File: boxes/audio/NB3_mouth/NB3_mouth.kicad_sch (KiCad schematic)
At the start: 3 parts, among them IC1 MAX98357AETE+T, J1 Conn_02x03_Odd_Even, J2 Conn_02x03_Odd_Even

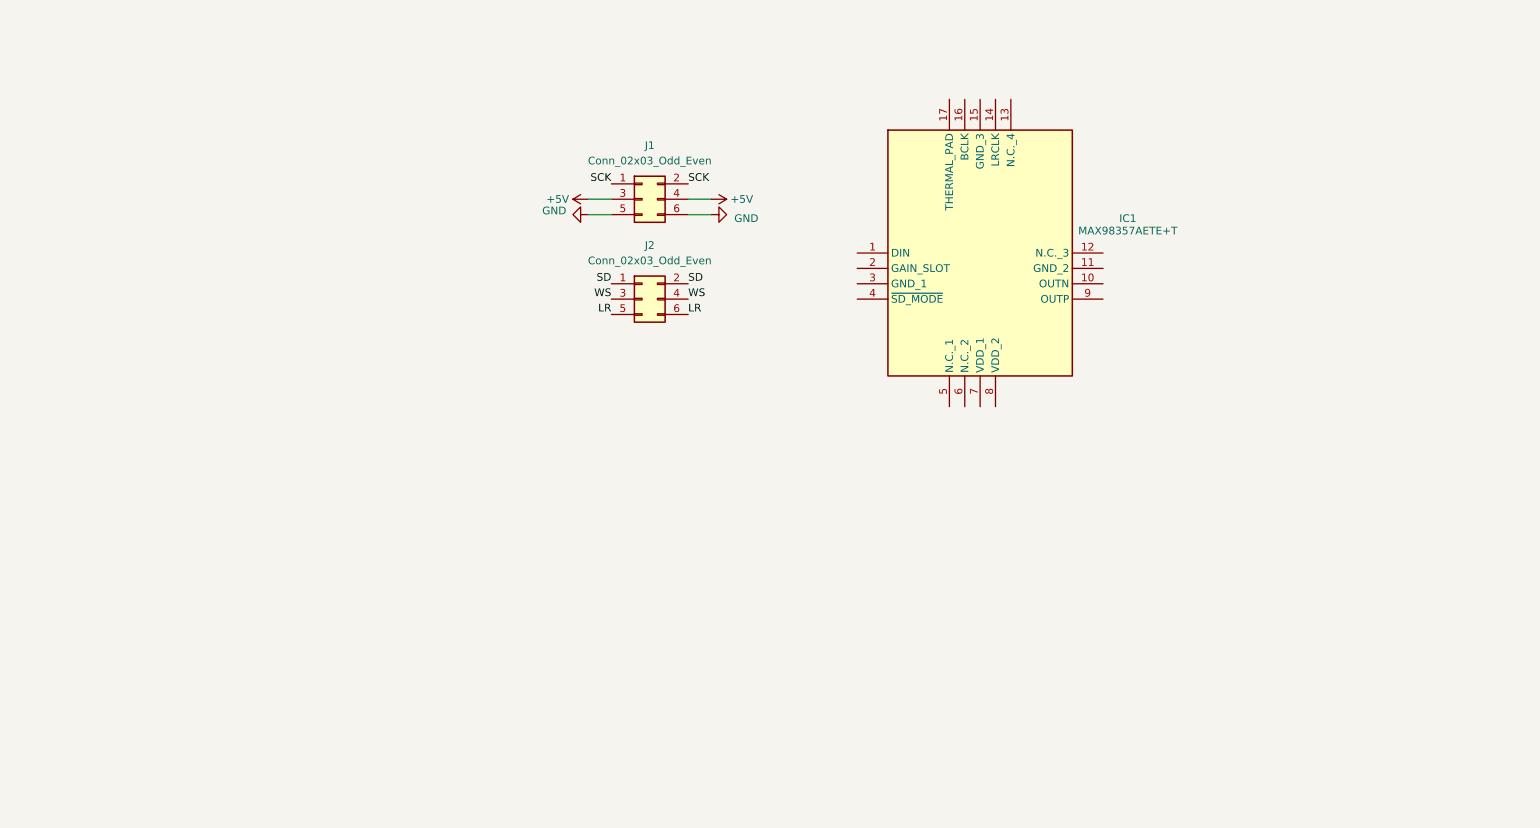
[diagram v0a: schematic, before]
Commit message: Tweak NB3_mouth
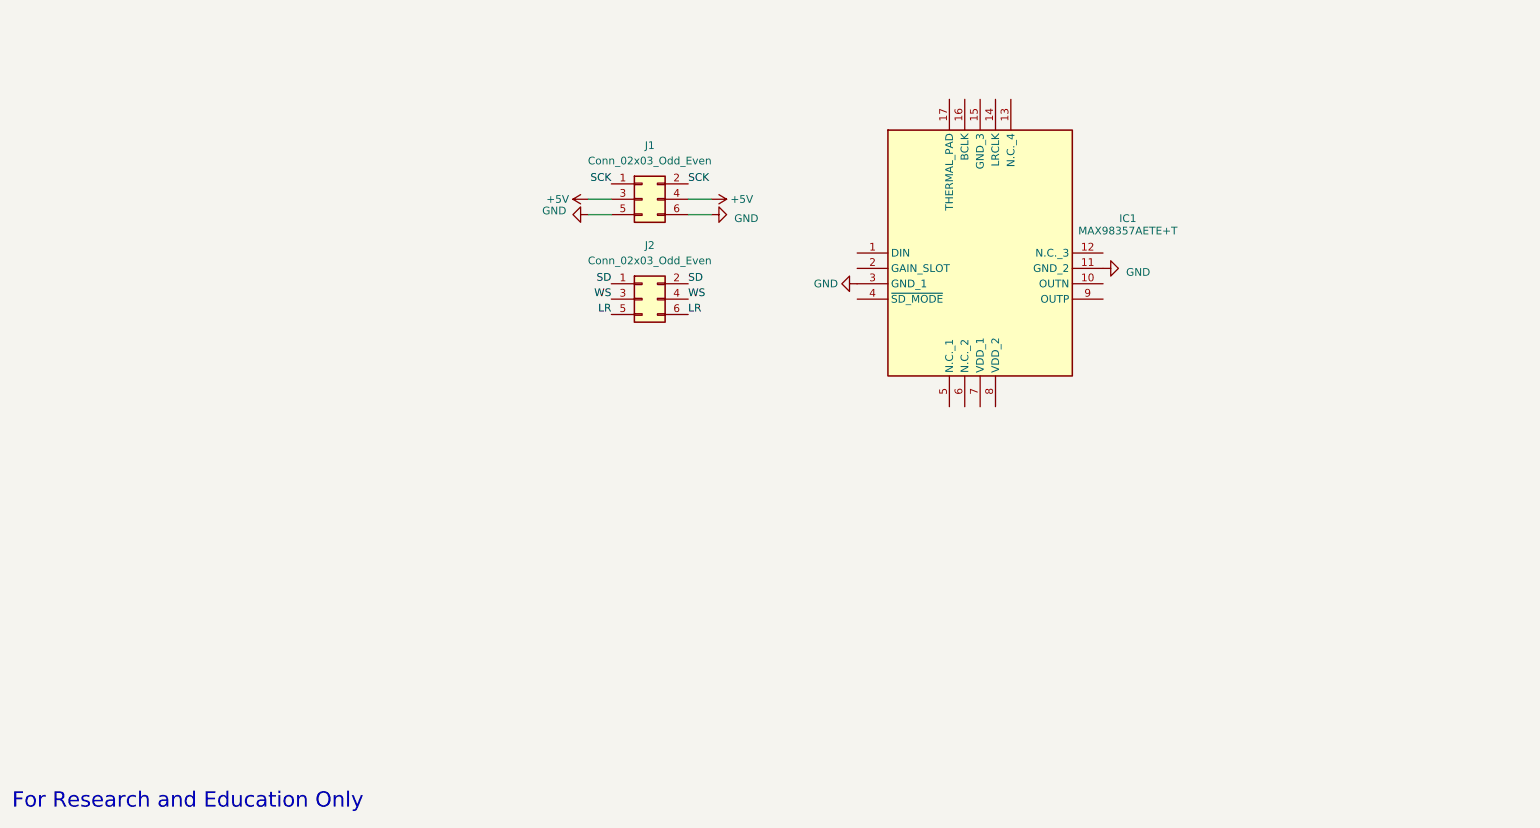
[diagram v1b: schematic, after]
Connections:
- net GND: now also IC1.11 (GND_2), IC1.3 (GND_1)
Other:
- note added: "For Research and Education Only"
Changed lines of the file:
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@@
     (stroke (width 0) (type solid))
   )
+  (text "For Research and Education Only" (at 15.24 194.945 0)
+    (effects (font (size 2.54 2.54) (color 0 0 0 1)) (justify left bottom))
+  )
   (label "LR" (at 114.3 113.03 180) (fields_autoplaced)
     (effects (font (size 1.27 1.27)) (justify right bottom))
@@
   (label "WS" (at 127 110.49 0) (fields_autoplaced)
     (effects (font (size 1.27 1.27)) (justify left bottom))
+  )
+  (symbol (lib_id "power:GND") (at 154.94 107.95 270) (unit 1)
+    (in_bom yes) (on_board yes) (dnp no) (fields_autoplaced)
+    (property "Reference" "#PWR06" (at 148.59 107.95 0)
+      (effects (font (size 1.27 1.27)) hide)
+    )
+    (property "Value" "GND" (at 151.7651 107.95 90)
+      (effects (font (size 1.27 1.27)) (justify right))
+    )
+    (property "Footprint" "" (at 154.94 107.95 0)
+      (effects (font (size 1.27 1.27)) hide)
+    )
+    (property "Datasheet" "" (at 154.94 107.95 0)
+      (effects (font (size 1.27 1.27)) hide)
+    )
+    (pin "1")
+    (instances
+      (project "NB3_mouth"
+        (path "/df27637c-d6c9-48ad-83e5-144198b72706"
+          (reference "#PWR06") (unit 1)
+        )
+      )
+    )
   )
   (symbol (lib_id "NB3_mouth:I2S_DAC-AMP_MAX98357A") (at 154.94 102.87 0) (unit 1)
@@
         )
       )
+    )
+  )
+  (symbol (lib_id "power:GND") (at 195.58 105.41 90) (unit 1)
+    (in_bom yes) (on_board yes) (dnp no) (fields_autoplaced)
+    (property "Reference" "#PWR05" (at 201.93 105.41 0)
+      (effects (font (size 1.27 1.27)) hide)
+    )
+    (property "Value" "GND" (at 199.39 106.0449 90)
+      (effects (font (size 1.27 1.27)) (justify right))
+    )
+    (property "Footprint" "" (at 195.58 105.41 0)
+      (effects (font (size 1.27 1.27)) hide)
+    )
+    (property "Datasheet" "" (at 195.58 105.41 0)
+      (effects (font (size 1.27 1.27)) hide)
+    )
+    (pin "1")
+    (instances
+      (project "NB3_mouth"
+        (path "/df27637c-d6c9-48ad-83e5-144198b72706"
+          (reference "#PWR05") (unit 1)
+        )
+      )

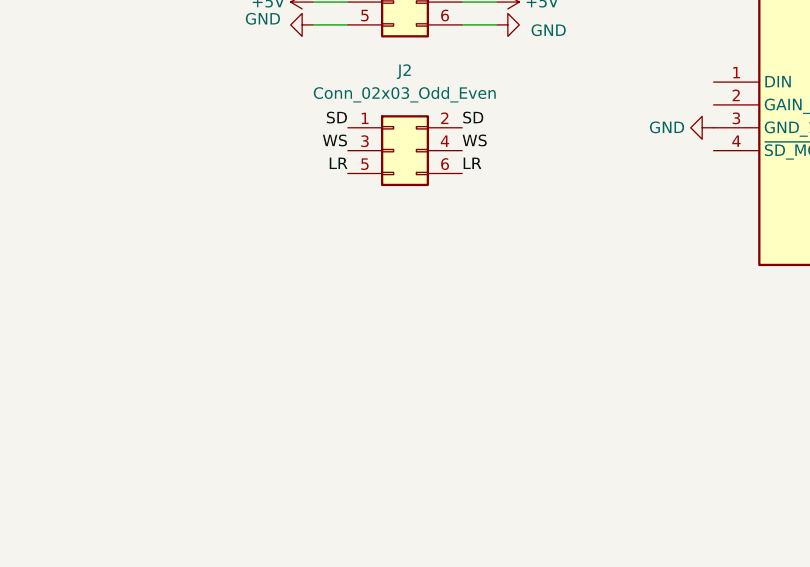
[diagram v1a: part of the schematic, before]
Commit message: Add JST connector to NB3_mouth
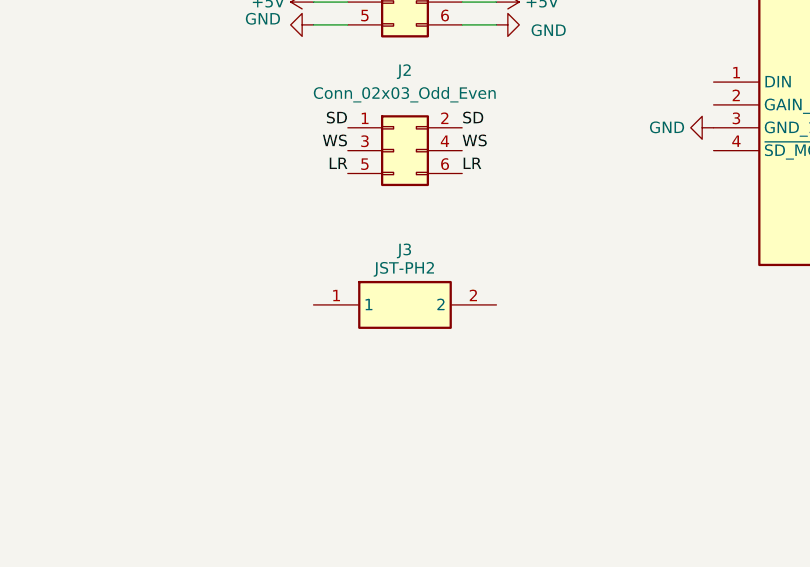
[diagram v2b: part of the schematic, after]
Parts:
- added J3: JST-PH2, NB3_mouth:Connector_Female_JST-PH2, symbol NB3_mouth:Connector_Female_JST-PH2
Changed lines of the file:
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@@
+    )
+  )
+  (symbol (lib_id "NB3_mouth:Connector_Female_JST-PH2") (at 110.49 127.635 0) (unit 1)
+    (in_bom yes) (on_board yes) (dnp no) (fields_autoplaced)
+    (property "Reference" "J3" (at 120.65 121.515 0)
+      (effects (font (size 1.27 1.27)))
+    )
+    (property "Value" " JST-PH2" (at 120.65 123.563 0)
+      (effects (font (size 1.27 1.27)))
+    )
+    (property "Footprint" "NB3_mouth:Connector_Female_JST-PH2" (at 127 222.555 0)
+      (effects (font (size 1.27 1.27)) (justify left top) hide)
+    )
+    (property "Datasheet" "https://cdn-shop.adafruit.com/datasheets/17311.pdf" (at 127 322.555 0)
+      (effects (font (size 1.27 1.27)) (justify left top) hide)
+    )
+    (property "Height" "" (at 127 522.555 0)
+      (effects (font (size 1.27 1.27)) (justify left top) hide)
+    )
+    (property "Mouser Part Number" "485-1769" (at 127 622.555 0)
+      (effects (font (size 1.27 1.27)) (justify left top) hide)
+    )
+    (property "Mouser Price/Stock" "https://www.mouser.co.uk/ProductDetail/Adafruit/1769?qs=GURawfaeGuBbgoGtf2XstA%3D%3D" (at 127 722.555 0)
+      (effects (font (size 1.27 1.27)) (justify left top) hide)
+    )
+    (property "Manufacturer_Name" "Adafruit" (at 127 822.555 0)
+      (effects (font (size 1.27 1.27)) (justify left top) hide)
+    )
+    (property "Manufacturer_Part_Number" "1769" (at 127 922.555 0)
+      (effects (font (size 1.27 1.27)) (justify left top) hide)
+    )
+    (pin "1")
+    (pin "2")
+    (instances
+      (project "NB3_mouth"
+        (path "/df27637c-d6c9-48ad-83e5-144198b72706"
+          (reference "J3") (unit 1)
+        )
+      )
     )
   )

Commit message: Upload NB3_ear "fab" v2
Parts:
- added R1, R2: R, Resistor_SMD:R_0402_1005Metric, symbol Device:R
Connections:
- net LR is gone; now on net Gain: J2.5 (Pin_5), J2.6 (Pin_6)
- net +5V: now also IC1.7 (VDD_1), IC1.8 (VDD_2), R1.1
- net GND: now also IC1.15 (GND_3), IC1.17 (THERMAL_PAD), R2.1
- net SCK: now also IC1.16 (BCLK)
- net SD: now also IC1.1 (DIN)
- net WS: now also IC1.14 (LRCLK)
- net Speaker-: now reaches IC1.10 (OUTN)
- net Speaker-: now also J3.2
- net Gain: now reaches IC1.2 (GAIN_SLOT)
- net at IC1.4 (~{SD_MODE}): now also R1.2, R2.2
- net Speaker+: now reaches IC1.9 (OUTP)
- net Speaker+: now also J3.1
- no-connect marks 0 -> 4
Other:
- moved on the sheet: IC1, J1, J2, J3

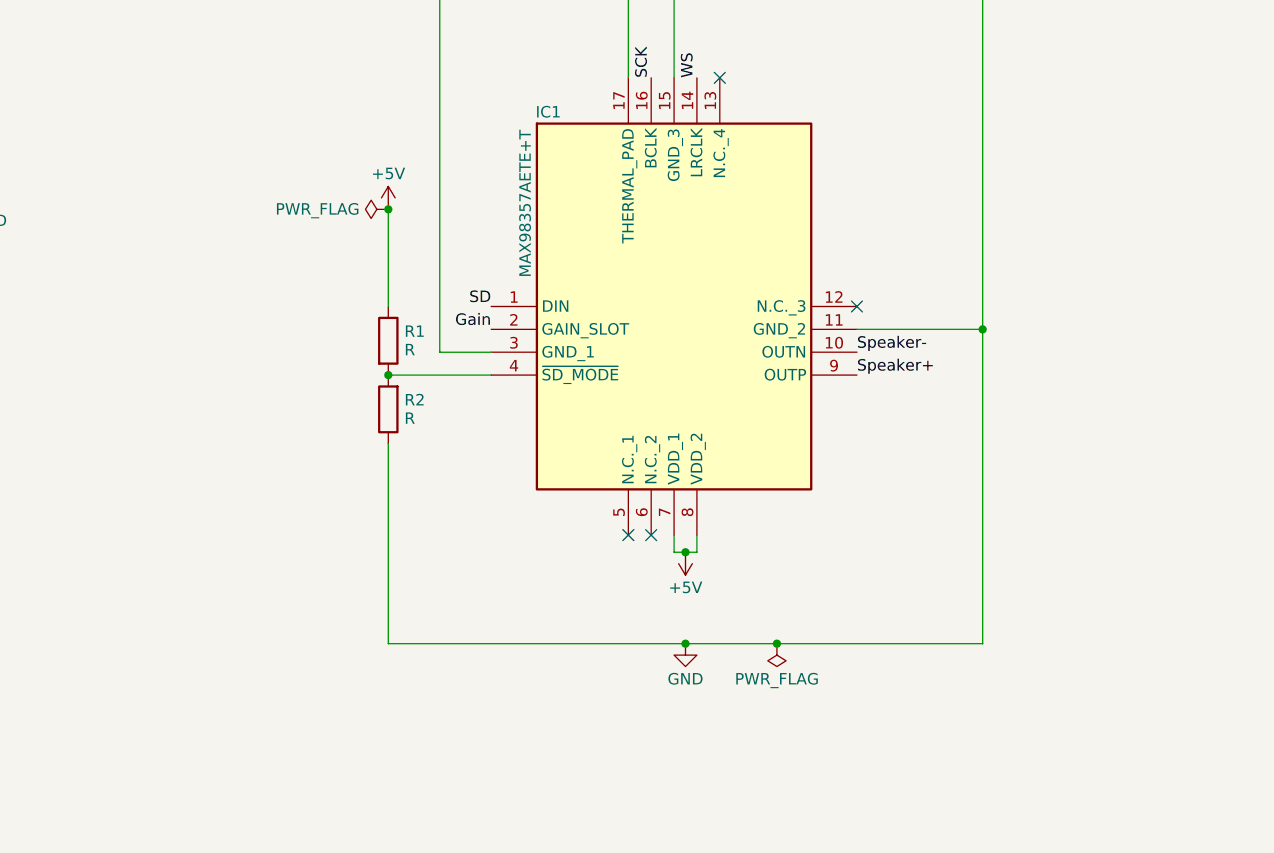
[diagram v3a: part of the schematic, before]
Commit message: Ref 1 of NB3 Mouth
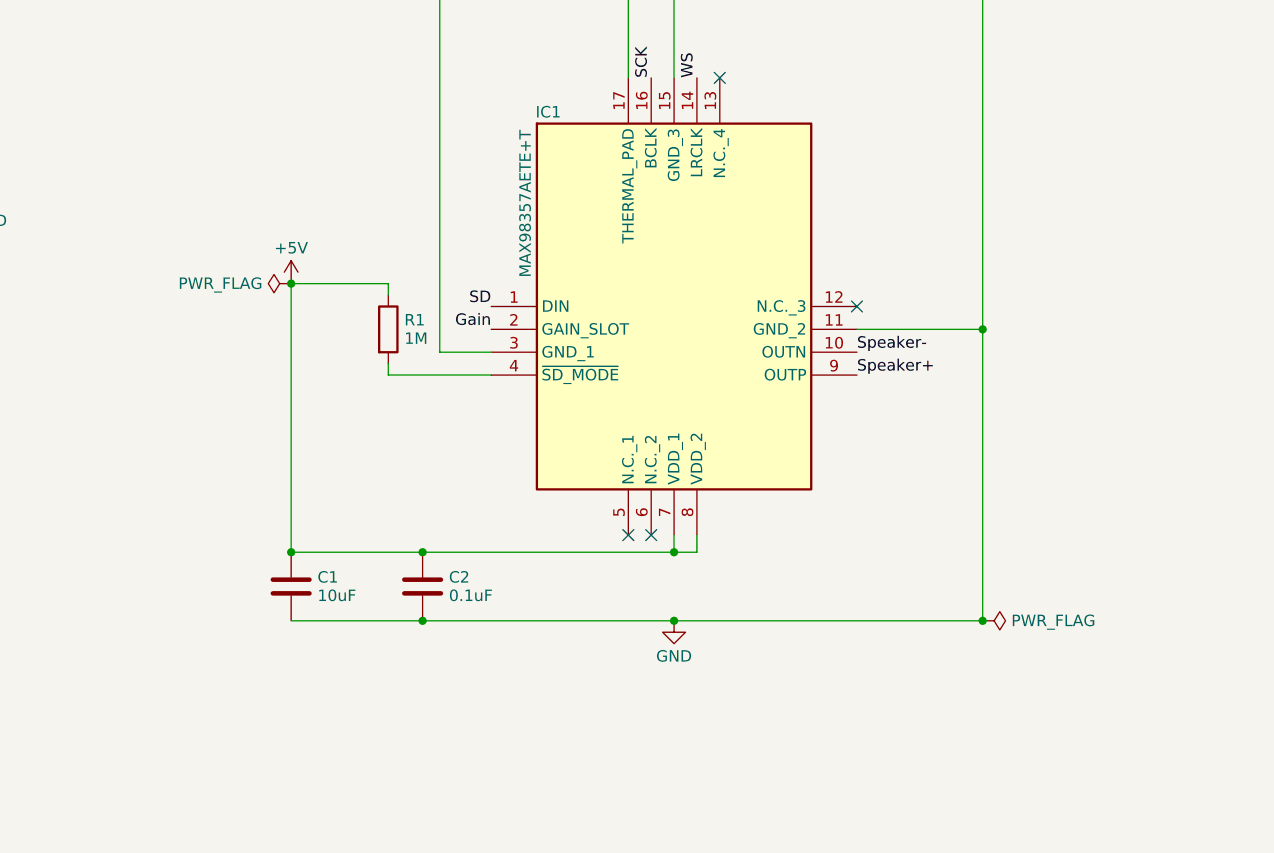
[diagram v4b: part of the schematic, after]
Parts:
- removed R2: R, Resistor_SMD:R_0402_1005Metric, symbol Device:R
- added C1: 10uF, Capacitor_SMD:C_0805_2012Metric, symbol Device:C
- added C2: 0.1uF, Capacitor_SMD:C_0402_1005Metric, symbol Device:C
- R1: value R -> 1M
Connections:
- net +5V: now also C1.1, C2.1
- net GND: now also C1.2, C2.2
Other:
- moved on the sheet: R1
